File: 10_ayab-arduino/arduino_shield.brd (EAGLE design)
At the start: 69.9 x 54.6 mm, 23 parts, among them IC3 PCF8574T, IC4 PCF8574T

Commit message: added gerber data for ayab-shield-v1.1 added kh-930 manual
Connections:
- new net DFG: ARD1.2
- new net QEWRT: ARD1.3
- net ENC0PINA: no longer ARD1.2
- net ENC0PINB: no longer ARD1.3
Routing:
- net ENC0PINB: track 26.6 -> 0.00 mm
- net ENC0PINA: track 26.1 -> 0.00 mm
- net QEWRT: track 0.00 -> 22.0 mm
- net DFG: track 0.00 -> 21.0 mm
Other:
- board text added: "KH-9xx"
- board text added: "www.ayab-knitting.com"
- board text removed: "KH 930 up"
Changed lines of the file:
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@@
 <text x="61.2775" y="45.4025" size="1.778" layer="25" font="vector" ratio="15" rot="R90">1</text>
 <text x="56.515" y="8.89" size="1.778" layer="25" font="vector" ratio="15" rot="R90">1</text>
-<text x="59.3725" y="26.035" size="1.778" layer="25" font="vector" ratio="15" rot="R90">KH 930 up</text>
+<text x="59.3725" y="27.305" size="1.778" layer="25" font="vector" ratio="15" rot="R90">KH-9xx</text>
+<text x="8.89" y="20.32" size="1.778" layer="25" font="vector" ratio="15">www.ayab-knitting.com</text>
 </plain>
 <attributes>
@@
 </element>
 <element name="JP5" library="pinheader_250" package="1X10" value="" x="52.705" y="34.6075" smashed="yes" rot="R270">
-<attribute name="NAME" x="49.4538" y="25.1587" size="1.27" layer="25" ratio="10" rot="R270"/>
+<attribute name="NAME" x="52.3113" y="21.3487" size="1.27" layer="25" ratio="10" rot="R270"/>
 <attribute name="VALUE" x="49.53" y="47.3075" size="1.27" layer="27" rot="R270"/>
 </element>
@@
 <element name="U$1" library="frames" package="A4L-LOC" value="" x="-81.5975" y="-52.3875"/>
 <element name="JP6" library="pinhead" package="1X02" value="" x="41.275" y="44.1325" rot="R90"/>
-<element name="S1" library="switch-tact" package="DTSM-6" value="DTSM-6" x="20.6375" y="2.8575"/>
-<element name="JP7" library="pinheader_250" package="1X03" value="" x="56.1975" y="23.1775" rot="R270"/>
+<element name="S1" library="switch-tact" package="DTSM-6" value="DTSM-6" x="20.6375" y="2.8575" smashed="yes">
+<attribute name="NAME" x="24.4475" y="2.2225" size="1.27" layer="25"/>
+</element>
+<element name="JP7" library="pinheader_250" package="1X03" value="" x="56.1975" y="23.1775" smashed="yes" rot="R270">
+<attribute name="NAME" x="55.8038" y="18.8087" size="1.27" layer="25" ratio="10" rot="R270"/>
+<attribute name="VALUE" x="53.0225" y="26.9875" size="1.27" layer="27" rot="R270"/>
+</element>
 <element name="JP8" library="pinheader_250" package="1X05" value="" x="56.1975" y="40.9575" rot="R270"/>
 </elements>
@@
 <wire x1="2.44" y1="7.3025" x2="2.54" y2="7.085" width="0.6096" layer="1"/>
 </signal>
-<signal name="ENC0PINA">
+<signal name="DFG">
 <contactref element="ARD1" pad="2"/>
-<contactref element="JP5" pad="4"/>
-<contactref element="JP8" pad="3"/>
-<wire x1="52.705" y1="38.3575" x2="52.9625" y2="38.3575" width="0.4064" layer="1"/>
-<wire x1="52.9625" y1="38.3575" x2="55.5625" y2="40.9575" width="0.4064" layer="1"/>
-<wire x1="55.5625" y1="40.9575" x2="56.1975" y2="40.9575" width="0.4064" layer="1"/>
 <wire x1="58.42" y1="50.8" x2="58.42" y2="48.26" width="0.4064" layer="1"/>
 <wire x1="58.42" y1="48.26" x2="57.4675" y2="47.3075" width="0.4064" layer="1"/>
@@
 <wire x1="50.165" y1="39.6875" x2="51.1175" y2="38.735" width="0.4064" layer="1"/>
 <wire x1="51.1175" y1="38.735" x2="52.3275" y2="38.735" width="0.4064" layer="1"/>
-<wire x1="52.3275" y1="38.735" x2="52.705" y2="38.3575" width="0.4064" layer="1"/>
 <wire x1="50.165" y1="46.6725" x2="50.8" y2="47.3075" width="0.4064" layer="1"/>
 </signal>
-<signal name="ENC0PINB">
+<signal name="QEWRT">
 <contactref element="ARD1" pad="3"/>
-<contactref element="JP5" pad="5"/>
-<contactref element="JP8" pad="4"/>
-<wire x1="56.1975" y1="38.4575" x2="55.92" y2="38.4575" width="0.4064" layer="1"/>
-<wire x1="55.92" y1="38.4575" x2="53.34" y2="35.8775" width="0.4064" layer="1"/>
-<wire x1="53.34" y1="35.8775" x2="52.725" y2="35.8775" width="0.4064" layer="1"/>
-<wire x1="52.725" y1="35.8775" x2="52.705" y2="35.8575" width="0.4064" layer="1"/>
 <wire x1="49.53" y1="46.99" x2="49.53" y2="37.7825" width="0.4064" layer="1"/>
 <wire x1="49.53" y1="37.7825" x2="51.435" y2="35.8775" width="0.4064" layer="1"/>
 <wire x1="51.435" y1="35.8775" x2="52.685" y2="35.8775" width="0.4064" layer="1"/>
-<wire x1="52.685" y1="35.8775" x2="52.705" y2="35.8575" width="0.4064" layer="1"/>
 <wire x1="49.53" y1="46.99" x2="50.4825" y2="47.9425" width="0.4064" layer="1"/>
 <wire x1="50.4825" y1="47.9425" x2="54.61" y2="47.9425" width="0.4064" layer="1"/>
@@
 <wire x1="33.02" y1="3.81" x2="33.02" y2="2.54" width="0.4064" layer="1"/>
 </signal>
+<signal name="ENC0PINA">
+<contactref element="JP5" pad="4"/>
+<contactref element="JP8" pad="3"/>
+<wire x1="52.705" y1="38.3575" x2="56.1975" y2="40.9575" width="0" layer="19" extent="1-1"/>
+</signal>
+<signal name="ENC0PINB">
+<contactref element="JP5" pad="5"/>
+<contactref element="JP8" pad="4"/>
+<wire x1="52.705" y1="35.8575" x2="56.1975" y2="38.4575" width="0" layer="19" extent="1-1"/>
+</signal>
 </signals>

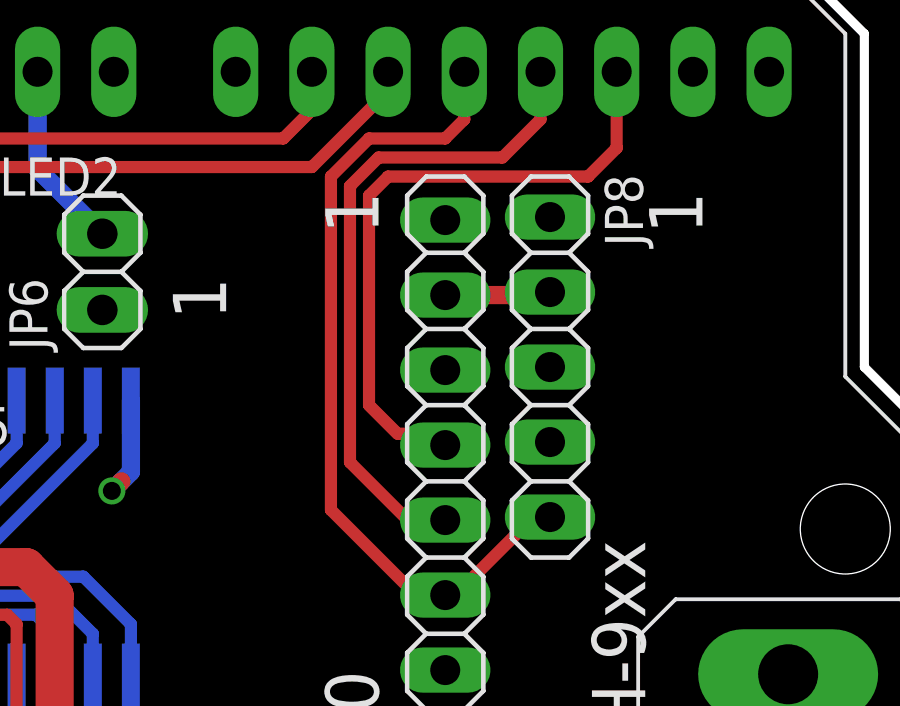
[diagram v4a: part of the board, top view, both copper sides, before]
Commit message: added defines for KH930 fixed pinning for S3 of KH930
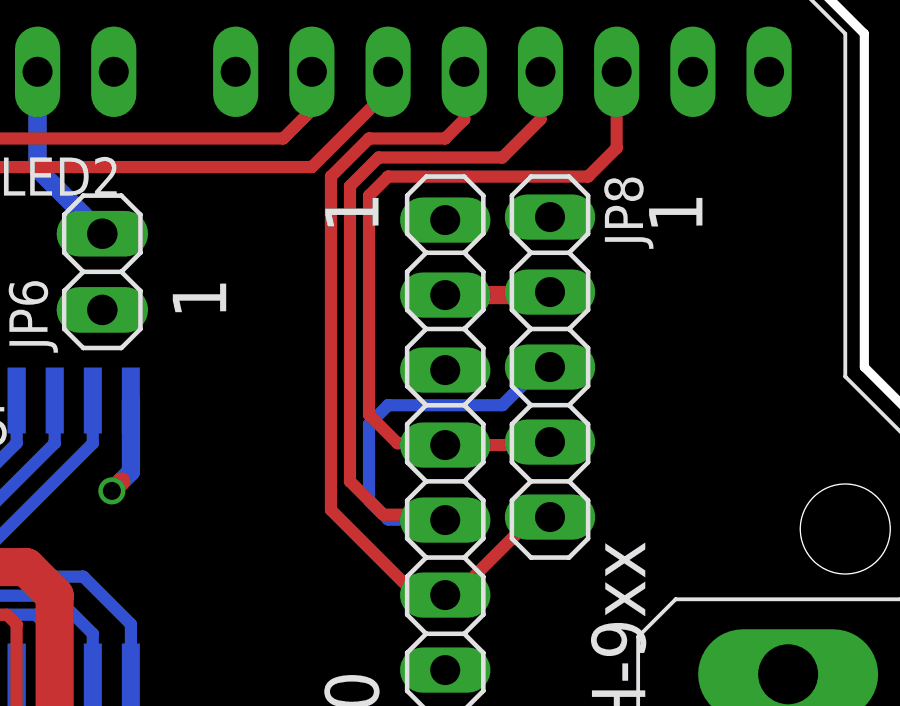
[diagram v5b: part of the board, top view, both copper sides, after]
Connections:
- removed net DFG: ARD1.2
- removed net QEWRT: ARD1.3
- net ENC0PINA: now also ARD1.2, JP8.4; no longer JP8.3
- net ENC0PINB: now also ARD1.3, JP8.3; no longer JP8.4
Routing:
- net ENC0PINB: track 0.00 -> 34.6 mm
- net ENC0PINA: track 0.00 -> 25.2 mm
- net QEWRT: track 22.0 -> 0.00 mm
- net DFG: track 21.0 -> 0.00 mm
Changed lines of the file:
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@@
 <layer number="123" name="tTestmark" color="7" fill="1" visible="no" active="yes"/>
 <layer number="124" name="bTestmark" color="7" fill="1" visible="no" active="yes"/>
-<layer number="125" name="_tNames" color="7" fill="1" visible="no" active="yes"/>
-<layer number="126" name="_bNames" color="7" fill="1" visible="no" active="yes"/>
-<layer number="127" name="_tValues" color="7" fill="1" visible="no" active="yes"/>
-<layer number="128" name="_bValues" color="7" fill="1" visible="no" active="yes"/>
+<layer number="125" name="_tNames" color="7" fill="1" visible="yes" active="yes"/>
+<layer number="126" name="_bNames" color="7" fill="1" visible="yes" active="yes"/>
+<layer number="127" name="_tValues" color="7" fill="1" visible="yes" active="yes"/>
+<layer number="128" name="_bValues" color="7" fill="1" visible="yes" active="yes"/>
 <layer number="131" name="tAdjust" color="7" fill="1" visible="no" active="yes"/>
 <layer number="132" name="bAdjust" color="7" fill="1" visible="no" active="yes"/>
@@
 <wire x1="2.44" y1="7.3025" x2="2.54" y2="7.085" width="0.6096" layer="1"/>
 </signal>
-<signal name="DFG">
-<contactref element="ARD1" pad="2"/>
-<wire x1="58.42" y1="50.8" x2="58.42" y2="48.26" width="0.4064" layer="1"/>
-<wire x1="58.42" y1="48.26" x2="57.4675" y2="47.3075" width="0.4064" layer="1"/>
-<wire x1="57.4675" y1="47.3075" x2="50.8" y2="47.3075" width="0.4064" layer="1"/>
-<wire x1="50.165" y1="46.6725" x2="50.165" y2="39.6875" width="0.4064" layer="1"/>
-<wire x1="50.165" y1="39.6875" x2="51.1175" y2="38.735" width="0.4064" layer="1"/>
-<wire x1="51.1175" y1="38.735" x2="52.3275" y2="38.735" width="0.4064" layer="1"/>
-<wire x1="50.165" y1="46.6725" x2="50.8" y2="47.3075" width="0.4064" layer="1"/>
-</signal>
-<signal name="QEWRT">
-<contactref element="ARD1" pad="3"/>
-<wire x1="49.53" y1="46.99" x2="49.53" y2="37.7825" width="0.4064" layer="1"/>
-<wire x1="49.53" y1="37.7825" x2="51.435" y2="35.8775" width="0.4064" layer="1"/>
-<wire x1="51.435" y1="35.8775" x2="52.685" y2="35.8775" width="0.4064" layer="1"/>
-<wire x1="49.53" y1="46.99" x2="50.4825" y2="47.9425" width="0.4064" layer="1"/>
-<wire x1="50.4825" y1="47.9425" x2="54.61" y2="47.9425" width="0.4064" layer="1"/>
-<wire x1="54.61" y1="47.9425" x2="55.88" y2="49.2125" width="0.4064" layer="1"/>
-<wire x1="55.88" y1="49.2125" x2="55.88" y2="50.8" width="0.4064" layer="1"/>
-</signal>
 <signal name="ENC0PINC">
 <contactref element="ARD1" pad="4"/>
@@
 <signal name="ENC0PINA">
 <contactref element="JP5" pad="4"/>
-<contactref element="JP8" pad="3"/>
-<wire x1="52.705" y1="38.3575" x2="56.1975" y2="40.9575" width="0" layer="19" extent="1-1"/>
+<contactref element="JP8" pad="4"/>
+<wire x1="52.705" y1="38.3575" x2="56.0975" y2="38.3575" width="0.4064" layer="1"/>
+<wire x1="56.0975" y1="38.3575" x2="56.1975" y2="38.4575" width="0.4064" layer="1"/>
+<contactref element="ARD1" pad="2"/>
+<wire x1="58.42" y1="50.8" x2="58.42" y2="48.26" width="0.4064" layer="1"/>
+<wire x1="58.42" y1="48.26" x2="57.4675" y2="47.3075" width="0.4064" layer="1"/>
+<wire x1="57.4675" y1="47.3075" x2="50.8" y2="47.3075" width="0.4064" layer="1"/>
+<wire x1="50.165" y1="46.6725" x2="50.165" y2="39.37" width="0.4064" layer="1"/>
+<wire x1="50.165" y1="46.6725" x2="50.8" y2="47.3075" width="0.4064" layer="1"/>
+<wire x1="50.165" y1="39.37" x2="51.1175" y2="38.4175" width="0.4064" layer="1"/>
+<wire x1="51.1175" y1="38.4175" x2="52.645" y2="38.4175" width="0.4064" layer="1"/>
+<wire x1="52.645" y1="38.4175" x2="52.705" y2="38.3575" width="0.4064" layer="1"/>
 </signal>
 <signal name="ENC0PINB">
 <contactref element="JP5" pad="5"/>
-<contactref element="JP8" pad="4"/>
-<wire x1="52.705" y1="35.8575" x2="56.1975" y2="38.4575" width="0" layer="19" extent="1-1"/>
+<contactref element="JP8" pad="3"/>
+<wire x1="56.1975" y1="40.9575" x2="55.88" y2="40.9575" width="0.4064" layer="16"/>
+<wire x1="55.88" y1="40.9575" x2="54.61" y2="39.6875" width="0.4064" layer="16"/>
+<wire x1="54.61" y1="39.6875" x2="50.8" y2="39.6875" width="0.4064" layer="16"/>
+<wire x1="50.8" y1="39.6875" x2="50.165" y2="39.0525" width="0.4064" layer="16"/>
+<wire x1="50.165" y1="39.0525" x2="50.165" y2="36.5125" width="0.4064" layer="16"/>
+<wire x1="50.165" y1="36.5125" x2="50.8" y2="35.8775" width="0.4064" layer="16"/>
+<wire x1="50.8" y1="35.8775" x2="52.685" y2="35.8775" width="0.4064" layer="16"/>
+<wire x1="52.685" y1="35.8775" x2="52.705" y2="35.8575" width="0.4064" layer="16"/>
+<contactref element="ARD1" pad="3"/>
+<wire x1="49.53" y1="46.99" x2="49.53" y2="37.1475" width="0.4064" layer="1"/>
+<wire x1="49.53" y1="46.99" x2="50.4825" y2="47.9425" width="0.4064" layer="1"/>
+<wire x1="50.4825" y1="47.9425" x2="54.61" y2="47.9425" width="0.4064" layer="1"/>
+<wire x1="54.61" y1="47.9425" x2="55.88" y2="49.2125" width="0.4064" layer="1"/>
+<wire x1="55.88" y1="49.2125" x2="55.88" y2="50.8" width="0.4064" layer="1"/>
+<wire x1="49.53" y1="37.1475" x2="50.64125" y2="36.03625" width="0.4064" layer="1"/>
+<wire x1="50.64125" y1="36.03625" x2="52.52625" y2="36.03625" width="0.4064" layer="1"/>
+<wire x1="52.52625" y1="36.03625" x2="52.705" y2="35.8575" width="0.4064" layer="1"/>
 </signal>
 </signals>

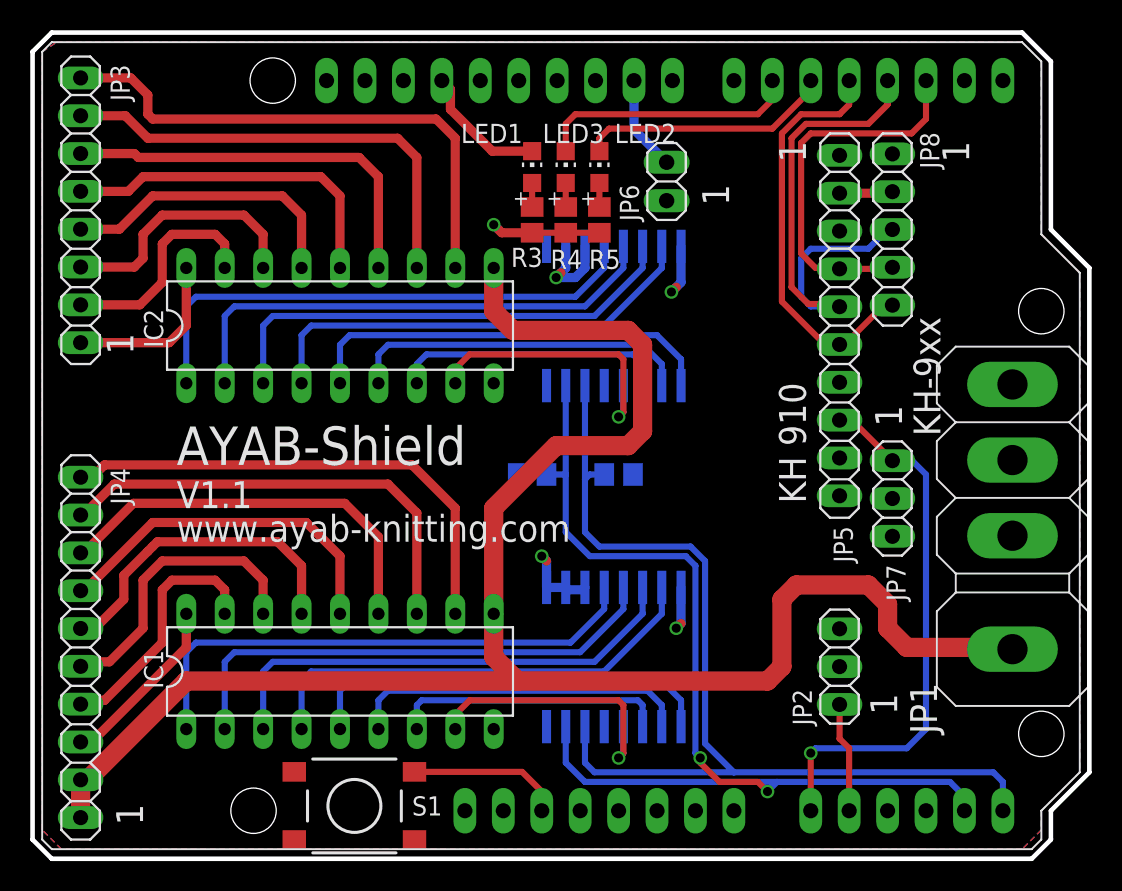
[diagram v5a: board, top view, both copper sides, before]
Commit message: Fixed Shield Layout (position of connectors)
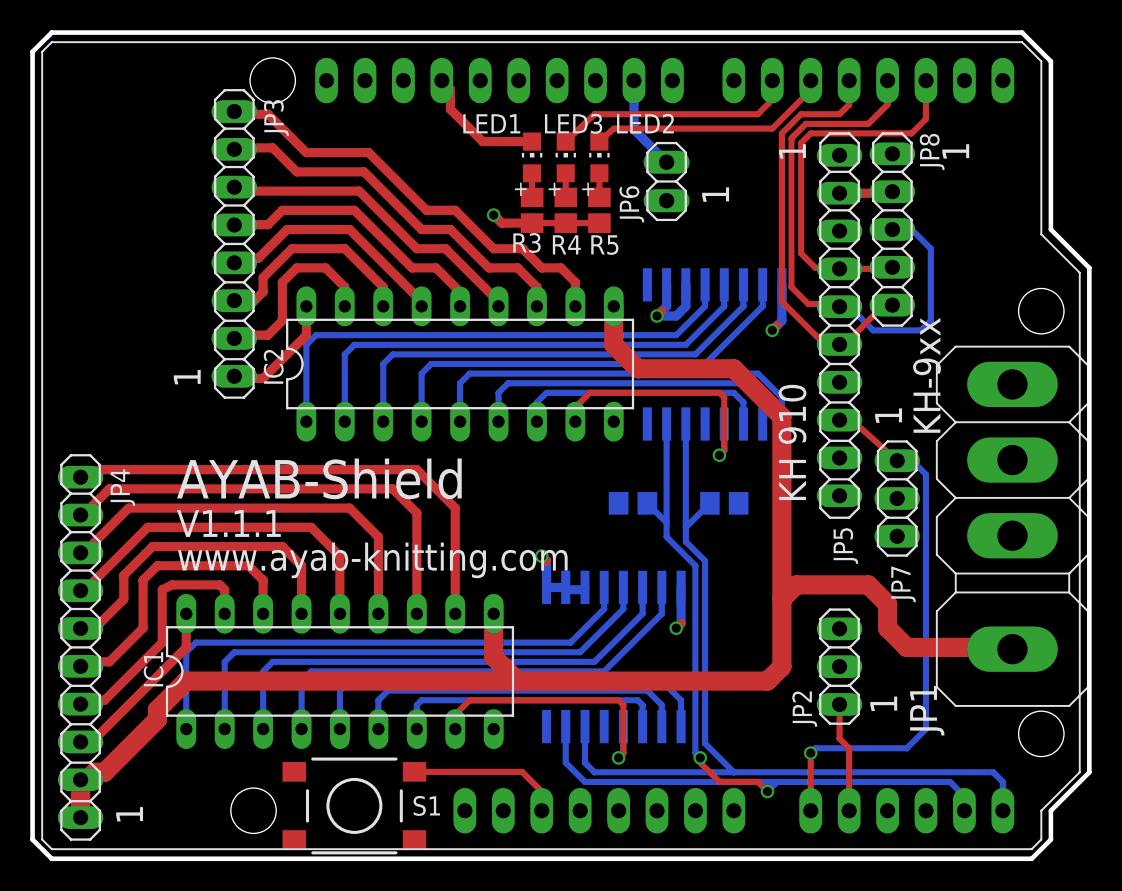
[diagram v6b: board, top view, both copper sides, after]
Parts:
- moved JP3 10.4 mm to (12.7, 40.0)
- moved IC2 8.33 mm to (27.6, 32.1)
- moved R2 7.24 mm to (45.1, 22.9)
- moved IC4 7.13 mm to (44.5, 32.7)
- moved R1 6.93 mm to (39.1, 22.9)
- moved LED1 0.63 mm to (32.4, 45.7)
- moved LED2 0.63 mm to (36.8, 45.7)
- moved LED3 0.63 mm to (34.6, 45.7)
- moved R3 0.63 mm to (32.4, 42.2)
- moved R4 0.63 mm to (34.6, 42.2)
- moved R5 0.63 mm to (36.8, 42.2)
- moved JP7 0.32 mm to (56.5, 23.2)
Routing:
- net +15V: track 118.1 -> 107.9 mm
- net SDA: track 70.3 -> 61.9 mm
- net SCL: track 67.0 -> 59.0 mm
- net N$24: track 35.7 -> 28.8 mm
- net N$23: track 30.7 -> 25.1 mm
- net N$22: track 26.4 -> 20.9 mm
- net N$21: track 22.8 -> 18.5 mm
- net N$20: track 19.5 -> 15.6 mm
- net N$17: track 11.3 -> 7.91 mm
- net N$19: track 17.2 -> 14.2 mm
- net ENC0PINB: track 34.6 -> 37.2 mm
- net N$18: track 14.8 -> 12.4 mm
- net N$35: track 17.4 -> 16.0 mm
- net N$15: track 18.1 -> 16.9 mm
- net N$14: track 22.9 -> 21.6 mm
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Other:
- board text added: "V1.1.1"
- board text removed: "V1.1"
